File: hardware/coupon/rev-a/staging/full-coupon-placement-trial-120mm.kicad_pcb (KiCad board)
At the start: 6 copper layers, 120 x 32.5 mm, 497 parts, among them J1 USB4505-03-0-A, J2 S2B-PH-SM4-TB, Q1 DMP2066LSN-7, Q10 DMP2066LSN-7, Q11 DMP2066LSN-7, Q12 DMP2066LSN-7, Q13 DMP2066LSN-7, Q14 DMP2066LSN-7, Q15 DMP2066LSN-7, Q16 DMP2066LSN-7, Q17 2N7002K-7, Q18 2N7002K-7, Q19 2N7002K-7, Q2 DMP2066LSN-7, Q20 2N7002K-7, Q21 2N7002K-7, Q22 2N7002K-7, Q23 2N7002K-7, Q24 2N7002K-7, Q25 2N7002K-7, Q26 2N7002K-7, Q27 2N7002K-7, Q28 2N7002K-7, Q29 2N7002K-7, Q3 DMP2066LSN-7, Q30 2N7002K-7, Q31 2N7002K-7, Q32 2N7002K-7, Q4 DMP2066LSN-7, Q5 DMP2066LSN-7, Q6 DMP2066LSN-7, Q7 DMP2066LSN-7, Q8 DMP2066LSN-7, Q9 DMP2066LSN-7, SW1 EVQP7J01P, SW2 JS202011JCQN, U1 TLC59581RTQT, U11 SN74LVC1G04DBVR, U17 SN74LVC1G11DBVR, U2 74HC4514PW,118, U23 SN74LVC1G06DBVR, U24 SN74LVC2G17DBVR, U25 SN74LVC2G17DBVR, U29 TPS70933DBVR, U3 ESP32-S3-WROOM-1U-N16R8, U31 TUSB320LAIRWBR, U32 TS3USB31ERSER, U33 TPD4E05U06DQAR, U34 TPS3808G01DBVR, U35 MAX17048G+T10, U36 TPS631000DRLR, U37 TPS63020DSJT, U38 2.5V shunt, U39 TMP390A2DRLR, U40 SN74AUP1G125DBVR, U41 BQ24074RGTR, U42 SN74AUP1G125DBVR, U43 SN74AUP1G125DBVR, U44 TPS259474ARPWR, U45 TPS259474ARPWR, U46 TCA9517ADGKR, U47 TPS3823A-33DBVR, U48 SN74LVC1G04DSFR, U49 SN74LVC1G74RSER, U50 SN74LVC1G74RSER, U51 SN74LVC1G11DRYR, U52 SN74LVC1G08DSFR, U53 TLV6700DSER, U54 SN74LVC2G00DCUR, U55 SN74LVC2G08DCUR

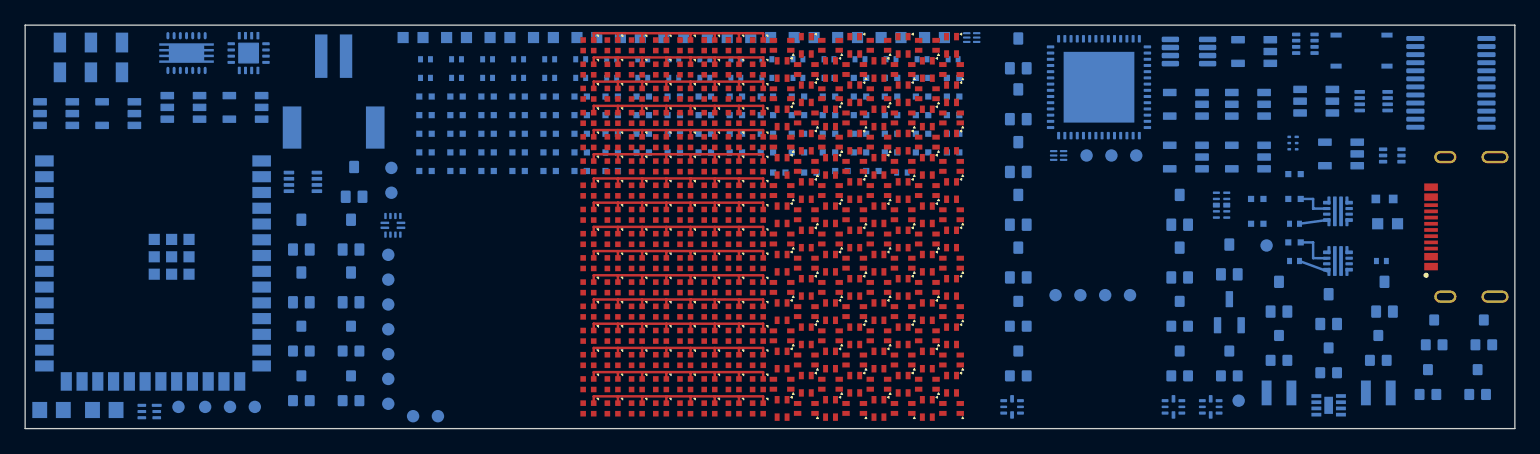
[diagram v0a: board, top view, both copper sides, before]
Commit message: Group and route VLED switching core in full coupon study
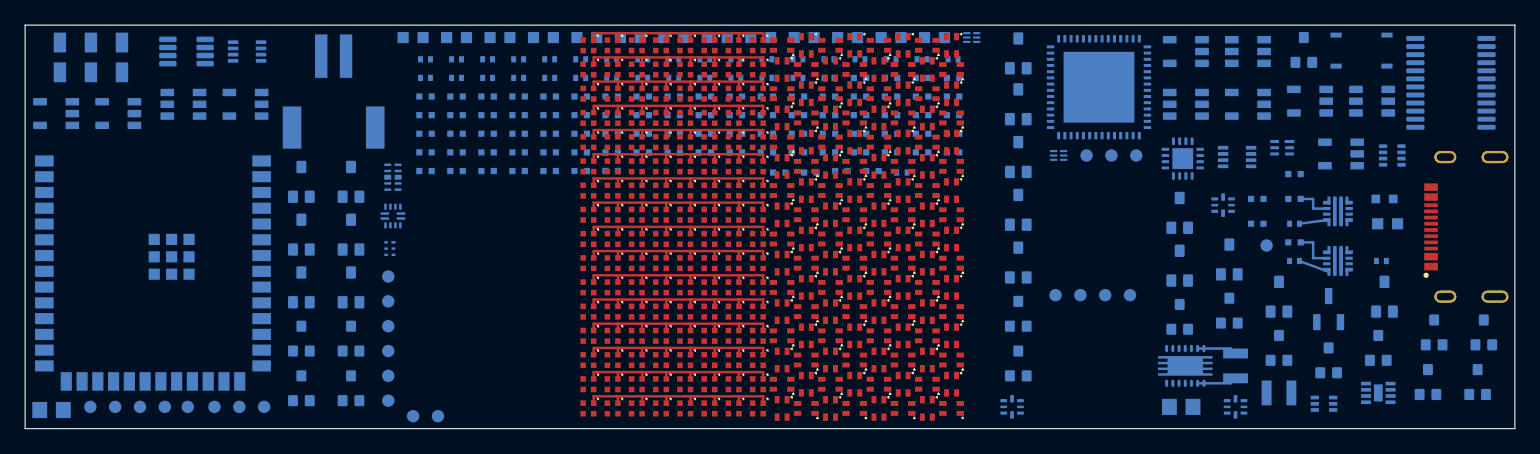
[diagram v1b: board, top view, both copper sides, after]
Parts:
- moved U42 103.6 mm to (2.50, 7.12)
- moved U53 93.7 mm to (101.2, 9.88)
- moved Q21 91.3 mm to (113.5, 24.8)
- moved Q22 91.3 mm to (117.5, 24.8)
- moved U34 91.0 mm to (93.5, 6.38)
- moved U40 91.0 mm to (98.5, 6.38)
- moved C42 91.0 mm to (93.1, 30.8)
- moved U54 90.8 mm to (17.9, 2.12)
- moved TP34 88.5 mm to (9.25, 30.8)
- moved U43 86.1 mm to (7.50, 7.12)
- moved U37 84.3 mm to (93.5, 27.4), turned to 0 degrees
- moved Q24 82.8 mm to (26.2, 25.2)
- moved U46 80.8 mm to (13.0, 2.12)
- moved Q23 78.8 mm to (22.2, 25.2)
- moved U41 75.7 mm to (93.2, 10.8)
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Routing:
- net Net-(L2-~-Pad2): track 0.00 -> 3.22 mm
- net Net-(L2-~-Pad1): track 0.00 -> 3.22 mm

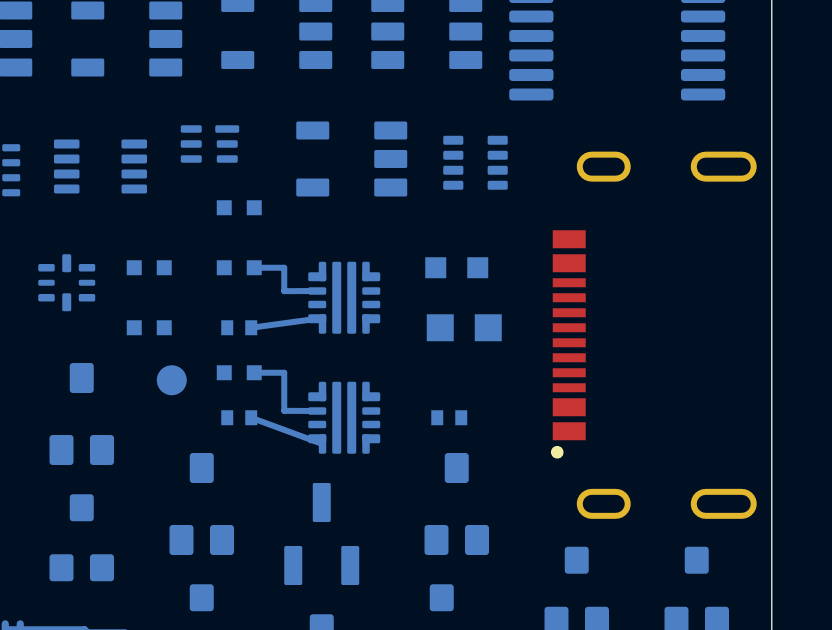
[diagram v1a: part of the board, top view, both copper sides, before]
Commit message: Trial routed USB VBUS entry and E0 bulk output on coupon board
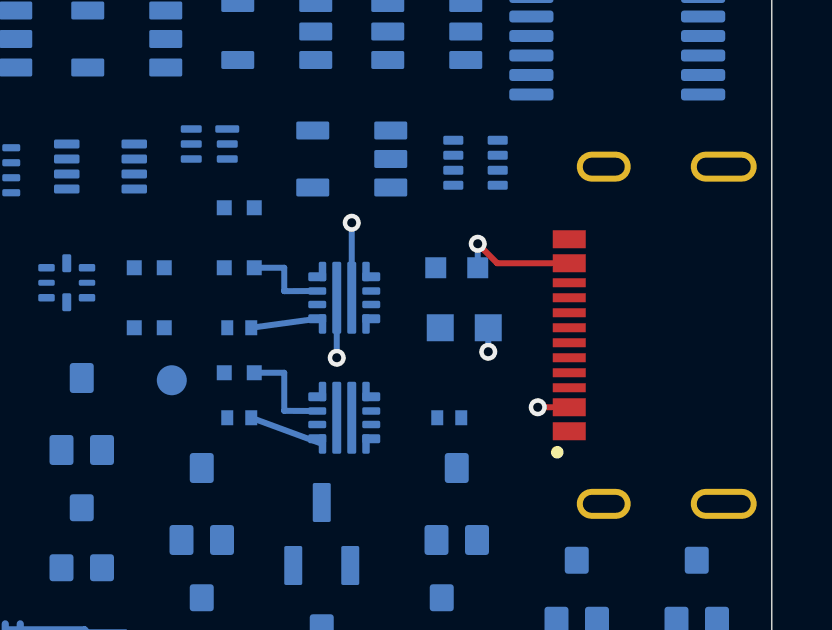
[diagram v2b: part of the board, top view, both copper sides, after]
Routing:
- net VBUS_CONNECTOR: track 0.00 -> 18.4 mm, vias 0 -> 3
- net +5V_USB: track 0.00 -> 7.93 mm, vias 0 -> 2
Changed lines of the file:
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@@
+	)
+	(segment
+		(start 105.5 15)
+		(end 105.5 17)
+		(width 0.2)
+		(layer "B.Cu")
+		(net "+5V_USB")
+	)
+	(segment
+		(start 105.5 17)
+		(end 110.35 17)
+		(width 0.2)
+		(layer "In4.Cu")
+		(net "+5V_USB")
+	)
+	(segment
+		(start 106 12.5)
+		(end 109.5 12.5)
+		(width 0.2)
+		(layer "In4.Cu")
+		(net "VBUS_CONNECTOR")
+	)
+	(segment
+		(start 106 15)
+		(end 106 12.5)
+		(width 0.2)
+		(layer "B.Cu")
+		(net "VBUS_CONNECTOR")
+	)
+	(segment
+		(start 109.5 12.5)
+		(end 110.2 13.2)
+		(width 0.2)
+		(layer "In4.Cu")
+		(net "VBUS_CONNECTOR")
+	)
+	(segment
+		(start 110.2 13.2)
+		(end 110.2 14)
+		(width 0.2)
+		(layer "B.Cu")
+		(net "VBUS_CONNECTOR")
+	)
+	(segment
+		(start 110.2 13.2)
+		(end 110.85 13.85)
+		(width 0.2)
+		(layer "F.Cu")
+		(net "VBUS_CONNECTOR")
+	)
+	(segment
+		(start 110.35 17)
+		(end 110.55 16.8)
+		(width 0.2)
+		(layer "In4.Cu")
+		(net "+5V_USB")
+	)
+	(segment
+		(start 110.55 16.8)
+		(end 110.55 16)
+		(width 0.2)
+		(layer "B.Cu")
+		(net "+5V_USB")
+	)
+	(segment
+		(start 110.85 13.85)
+		(end 113.25 13.85)
+		(width 0.2)
+		(layer "F.Cu")
+		(net "VBUS_CONNECTOR")
+	)
+	(segment
+		(start 112.2 15.2)
+		(end 110.2 13.2)
+		(width 0.2)
+		(layer "In4.Cu")
+		(net "VBUS_CONNECTOR")
+	)
+	(segment
+		(start 112.2 18.65)
+		(end 112.2 15.2)
+		(width 0.2)
+		(layer "In4.Cu")
+		(net "VBUS_CONNECTOR")
+	)
+	(segment
+		(start 113.25 18.65)
+		(end 112.2 18.65)
+		(width 0.2)
+		(layer "F.Cu")
+		(net "VBUS_CONNECTOR")
 	)
 	(segment
@@
 		(net "Net-(L2-~-Pad2)")
 	)
+	(via
+		(at 105.5 17)
+		(size 0.6)
+		(drill 0.3)
+		(layers "F.Cu" "B.Cu")
+		(net "+5V_USB")
+	)
+	(via
+		(at 106 12.5)
+		(size 0.6)
+		(drill 0.3)
+		(layers "F.Cu" "B.Cu")
+		(net "VBUS_CONNECTOR")
+	)
+	(via
+		(at 110.2 13.2)
+		(size 0.6)
+		(drill 0.3)
+		(layers "F.Cu" "B.Cu")
+		(net "VBUS_CONNECTOR")
+	)
+	(via
+		(at 110.55 16.8)
+		(size 0.6)
+		(drill 0.3)
+		(layers "F.Cu" "B.Cu")
+		(net "+5V_USB")
+	)
+	(via
+		(at 112.2 18.65)
+		(size 0.6)
+		(drill 0.3)
+		(layers "F.Cu" "B.Cu")
+		(net "VBUS_CONNECTOR")
+	)
 	(embedded_fonts no)

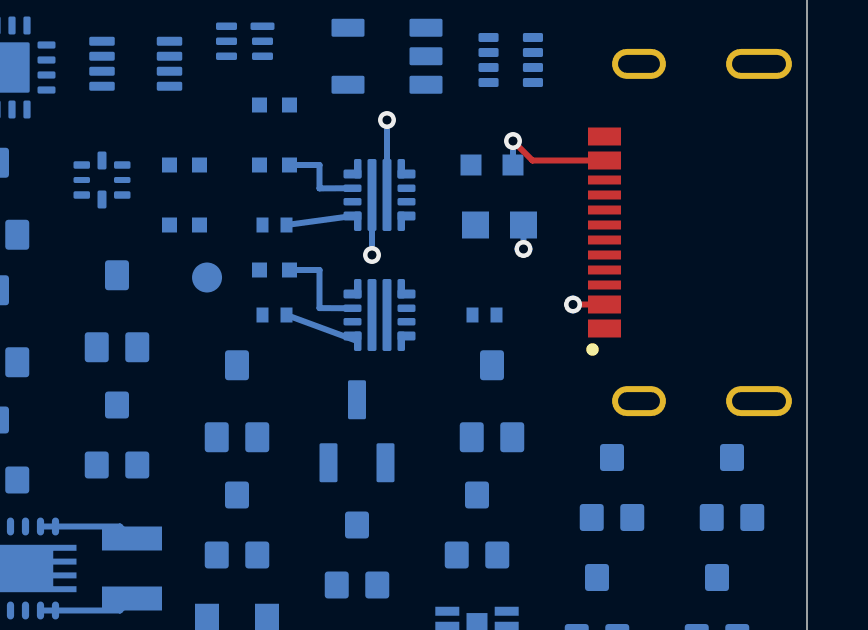
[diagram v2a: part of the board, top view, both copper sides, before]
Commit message: Connect E1 input and local charger capacitor in board study
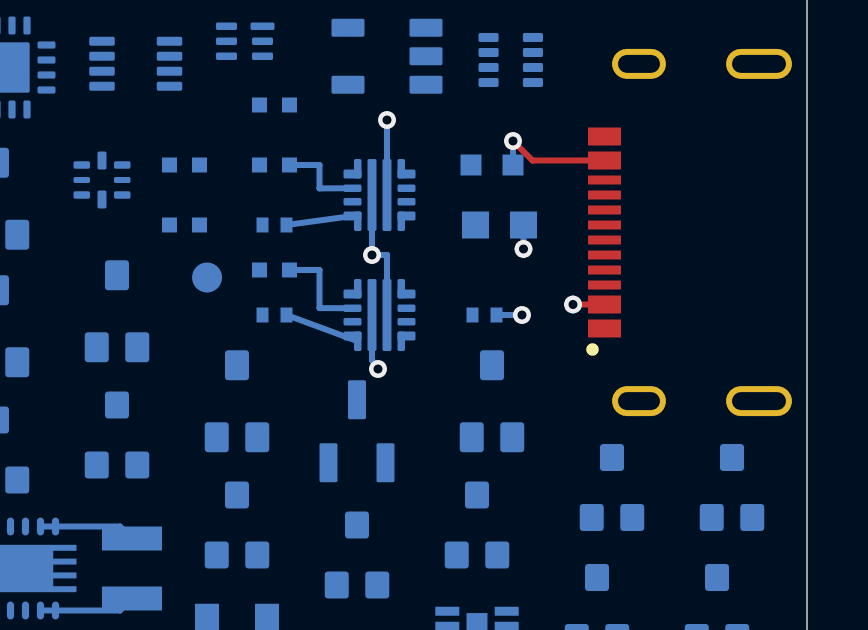
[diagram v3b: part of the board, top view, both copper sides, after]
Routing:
- net CHARGER_IN_DRAFT: track 0.00 -> 8.26 mm, vias 0 -> 2
- net +5V_USB: track 7.93 -> 10.4 mm
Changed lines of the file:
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@@
+	)
+	(segment
+		(start 105.5 19)
+		(end 105.5 20.5)
+		(width 0.2)
+		(layer "B.Cu")
+		(net "CHARGER_IN_DRAFT")
+	)
+	(segment
+		(start 105.5 20.5)
+		(end 105.7 20.8)
+		(width 0.2)
+		(layer "B.Cu")
+		(net "CHARGER_IN_DRAFT")
+	)
+	(segment
+		(start 105.7 20.8)
+		(end 108.7 20.8)
+		(width 0.2)
+		(layer "In4.Cu")
+		(net "CHARGER_IN_DRAFT")
 	)
 	(segment
@@
 	)
 	(segment
+		(start 106 17)
+		(end 105.5 17)
+		(width 0.2)
+		(layer "B.Cu")
+		(net "+5V_USB")
+	)
+	(segment
+		(start 106 19)
+		(end 106 17)
+		(width 0.2)
+		(layer "B.Cu")
+		(net "+5V_USB")
+	)
+	(segment
+		(start 108.7 20.8)
+		(end 110.5 19)
+		(width 0.2)
+		(layer "In4.Cu")
+		(net "CHARGER_IN_DRAFT")
+	)
+	(segment
 		(start 109.5 12.5)
 		(end 110.2 13.2)
@@
 		(layer "In4.Cu")
 		(net "+5V_USB")
+	)
+	(segment
+		(start 110.5 19)
+		(end 109.65 19)
+		(width 0.2)
+		(layer "B.Cu")
+		(net "CHARGER_IN_DRAFT")
 	)
 	(segment
@@
 	)
 	(via
+		(at 105.7 20.8)
+		(size 0.6)
+		(drill 0.3)
+		(layers "F.Cu" "B.Cu")
+		(net "CHARGER_IN_DRAFT")
+	)
+	(via
 		(at 106 12.5)
 		(size 0.6)
@@
 	)
 	(via
+		(at 110.5 19)
+		(size 0.6)
+		(drill 0.3)
+		(layers "F.Cu" "B.Cu")
+		(net "CHARGER_IN_DRAFT")
+	)
+	(via

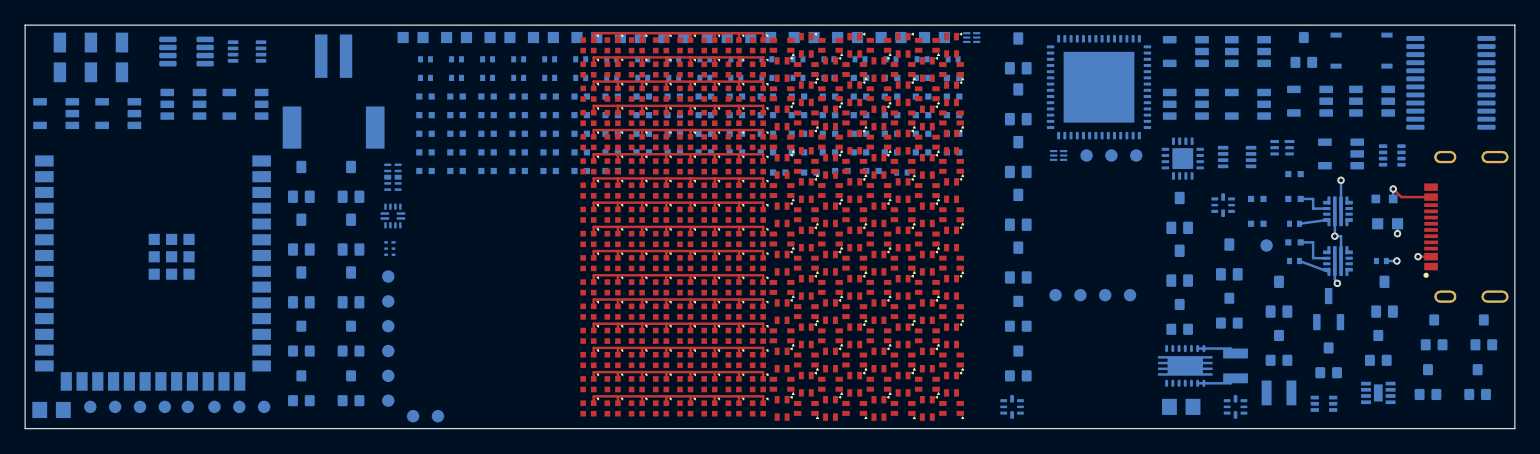
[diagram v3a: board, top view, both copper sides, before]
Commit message: Regroup charger input and bulk capacitor beside E1 path
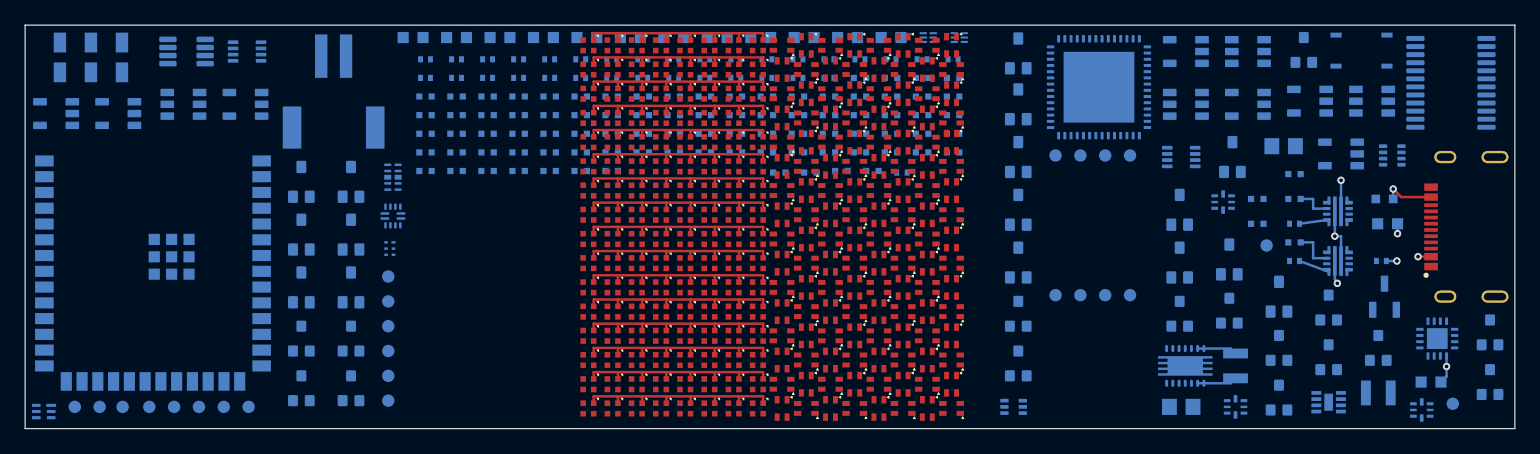
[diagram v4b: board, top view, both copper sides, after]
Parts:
- moved TP33 107.8 mm to (115.0, 30.5)
- moved U53 102.0 mm to (1.50, 31.1)
- moved Q30 94.8 mm to (22.2, 29.2)
- moved C43 91.0 mm to (93.1, 30.8)
- moved Q12 75.0 mm to (97.2, 10.6)
- moved Q32 74.8 mm to (101.0, 30.0)
- moved Q8 74.8 mm to (26.2, 21.1)
- moved TP13 70.8 mm to (100.0, 17.8)
- moved Q16 70.8 mm to (93.0, 14.9)
- moved Q3 70.8 mm to (26.2, 16.9)
- moved Q6 70.8 mm to (93.0, 19.1)
- moved TP22 59.8 mm to (89.0, 21.8)
- moved Q14 53.8 mm to (26.2, 12.6)
- moved TP14 53.8 mm to (29.3, 20.2)
- moved C56 48.7 mm to (113.2, 28.8)
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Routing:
- net CHARGER_IN_DRAFT: track 8.26 -> 20.7 mm, vias 2 -> 3
